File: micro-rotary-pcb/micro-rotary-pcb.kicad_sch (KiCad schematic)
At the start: 12 parts, among them P1 speed, U1 L7805

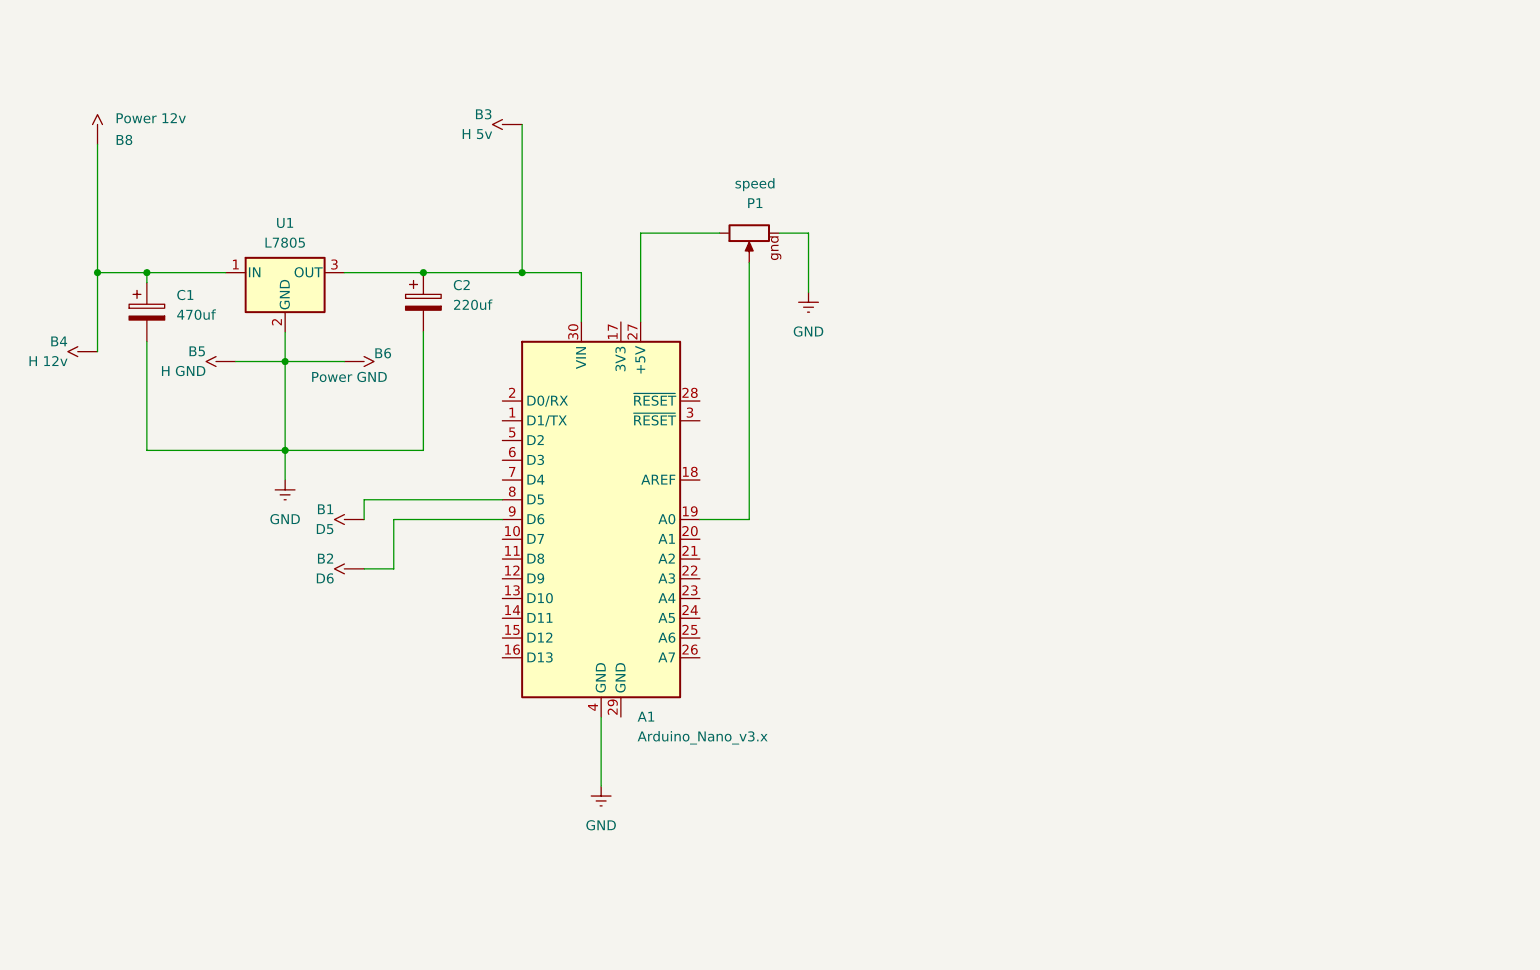
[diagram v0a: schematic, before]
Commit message: change arduino e potentiometer footprint
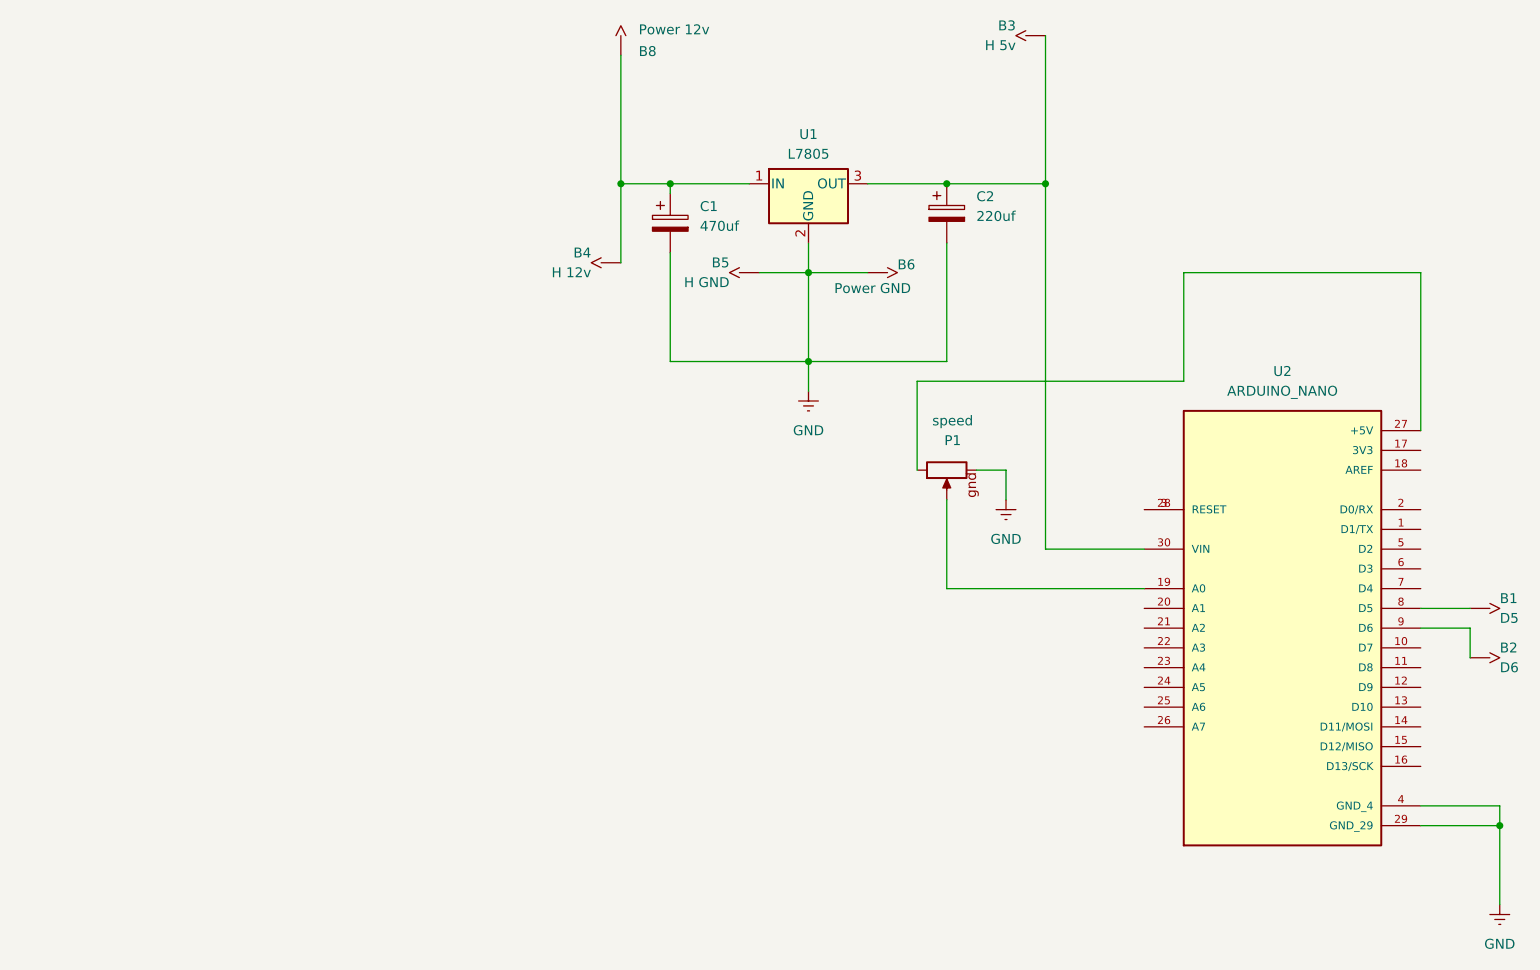
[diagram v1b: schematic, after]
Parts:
- removed A1: Arduino_Nano_v3.x, Module:Arduino_Nano, symbol MCU_Module:Arduino_Nano_v3.x
- added U2: ARDUINO_NANO, Arduino:ARDUINO_NANO, symbol Arduino:ARDUINO_NANO
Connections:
- net GND: now also U2.29 (GND_29), U2.4 (GND_4)
- net at P1.1: now also U2.27 (+5V)
- net at P1.2: now also U2.19 (A0)
- net at B3.1, C2.1, U1.3 (OUT): now also U2.30 (VIN)
- net at B2.1: now also U2.9 (D6)
- net at B1.1: now also U2.8 (D5)
- new net: U2.28 (RESET), U2.3 (RESET)
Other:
- moved on the sheet: B1, B2, B3, B4, B5, B6, B8, C1, C2, P1, U1
